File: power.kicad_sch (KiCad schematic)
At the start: 14 parts

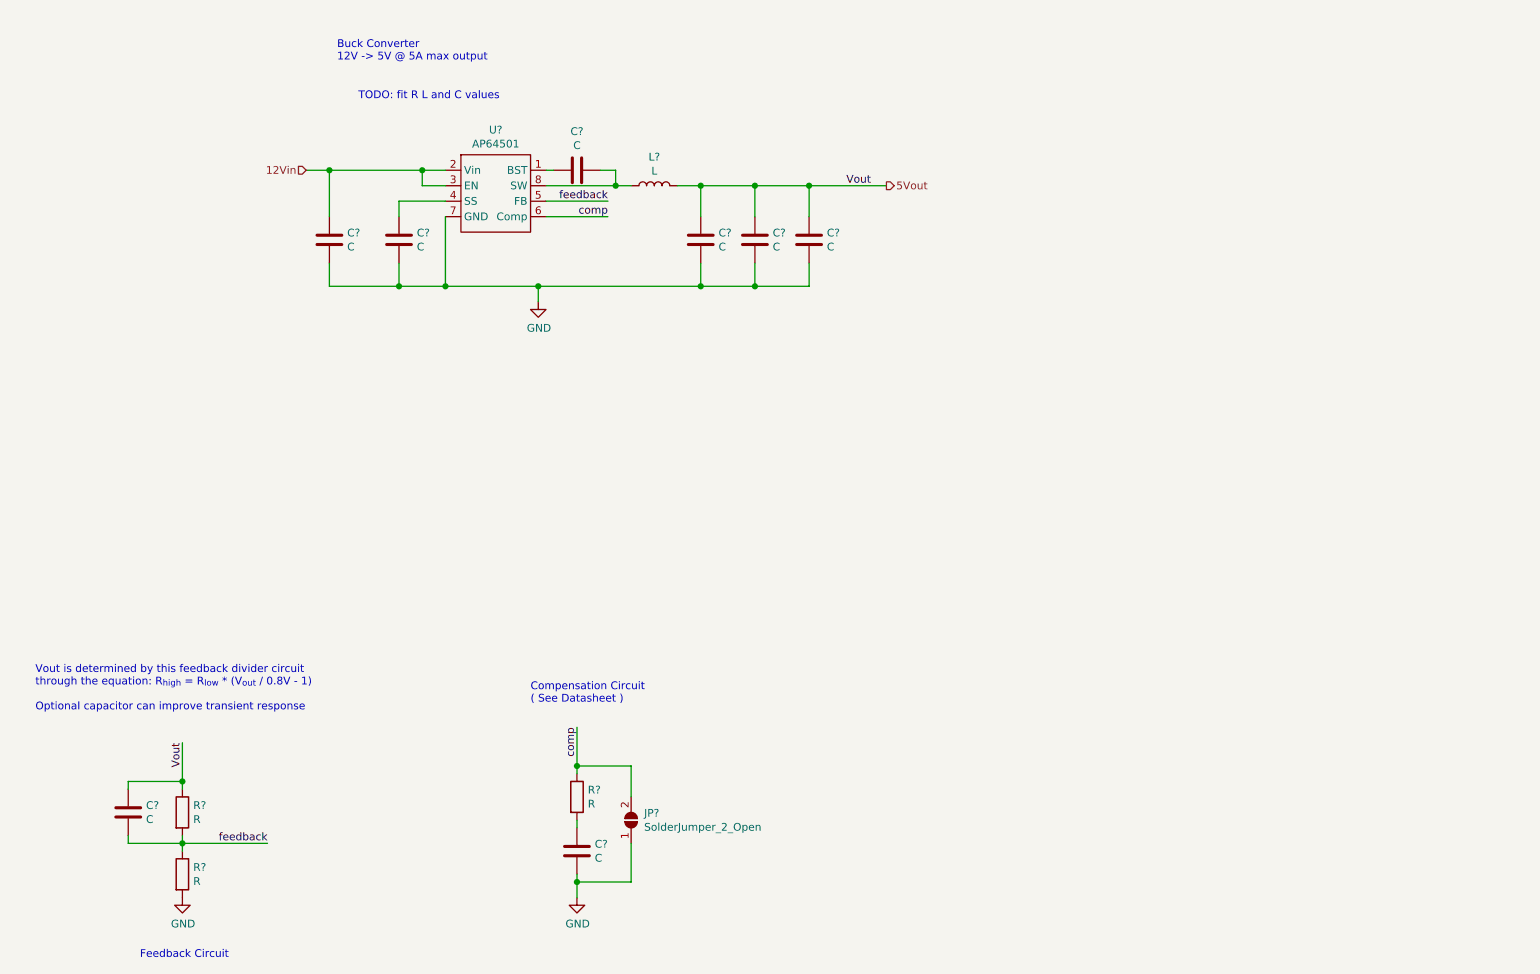
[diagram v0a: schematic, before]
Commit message: Added LC values and inductor part number to buck converter circuit
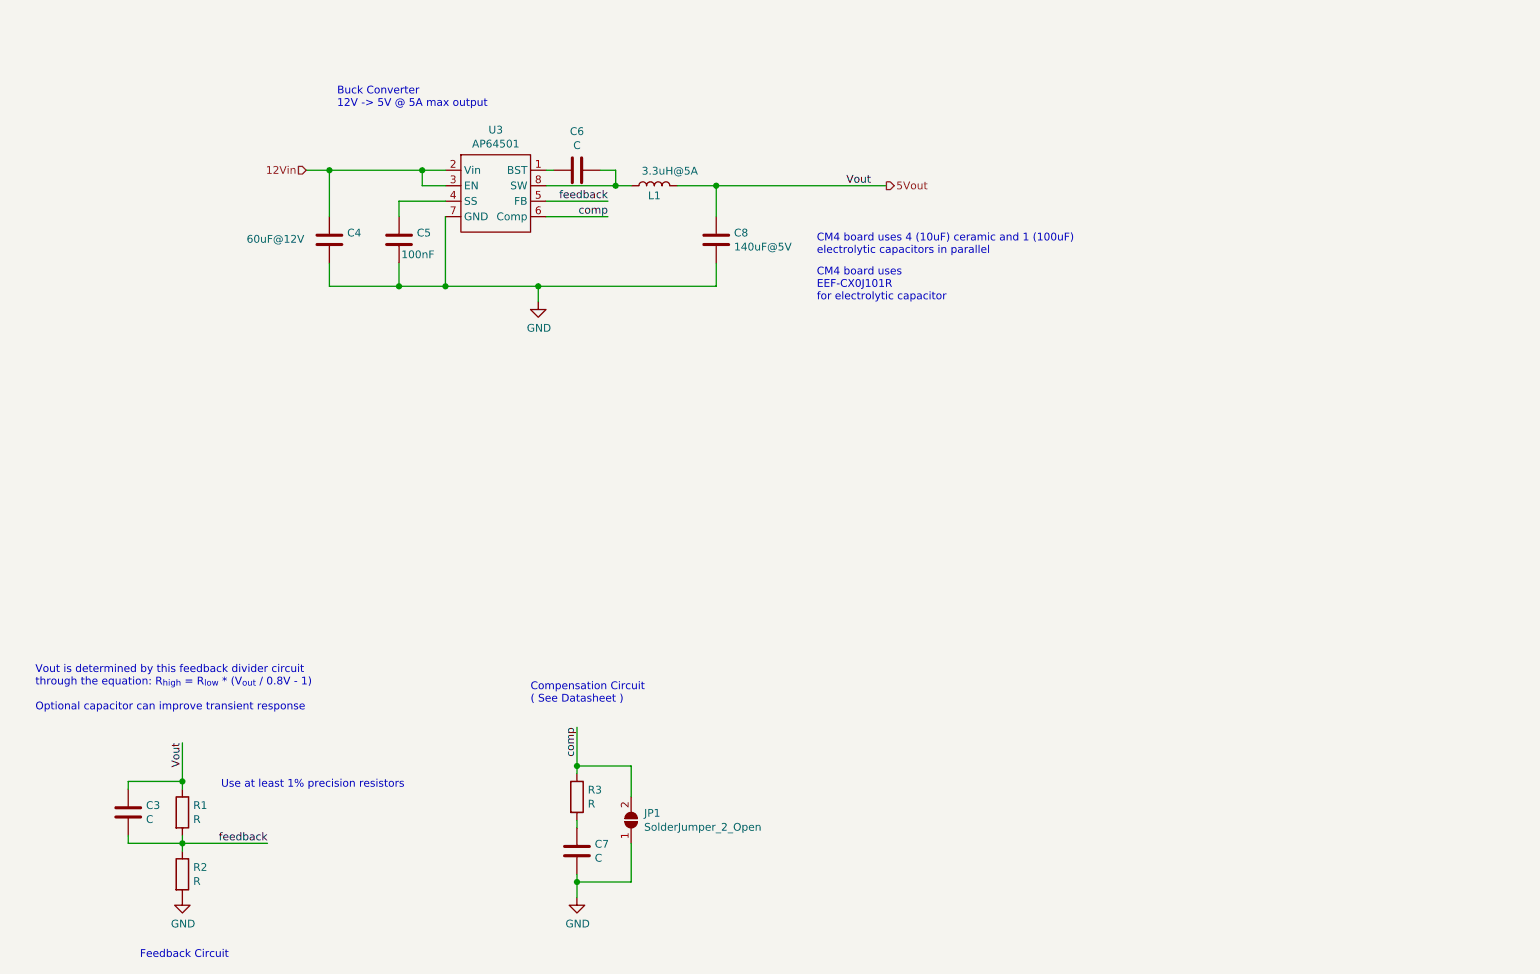
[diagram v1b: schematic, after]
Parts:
- removed C? (x2): C, symbol Device:C
- removed L?: L, symbol Device:L
- added L1: 3.3uH@5A, symbol symbols:3.3uH
- C4: renamed from C?; value C -> 60uF@12V
- C5: renamed from C?; value C -> 100nF
- C8: renamed from C?; value C -> 140uF@5V
- gave numbers to parts that had none: 8
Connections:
- net 5Vout: now also L1.2
- net at C6.2, U3.8 (SW): now also L1.1
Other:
- note added: "CM4 board uses 4 (10uF) ceramic and 1 (100uF) electrolytic capacitors in parallel"
- note added: "CM4 board uses EEF-CX0J101R for electrolytic capacitor"
- note added: "Use at least 1% precision resistors"
- note removed: "TODO: fit R L and C values"
- moved on the sheet: C8

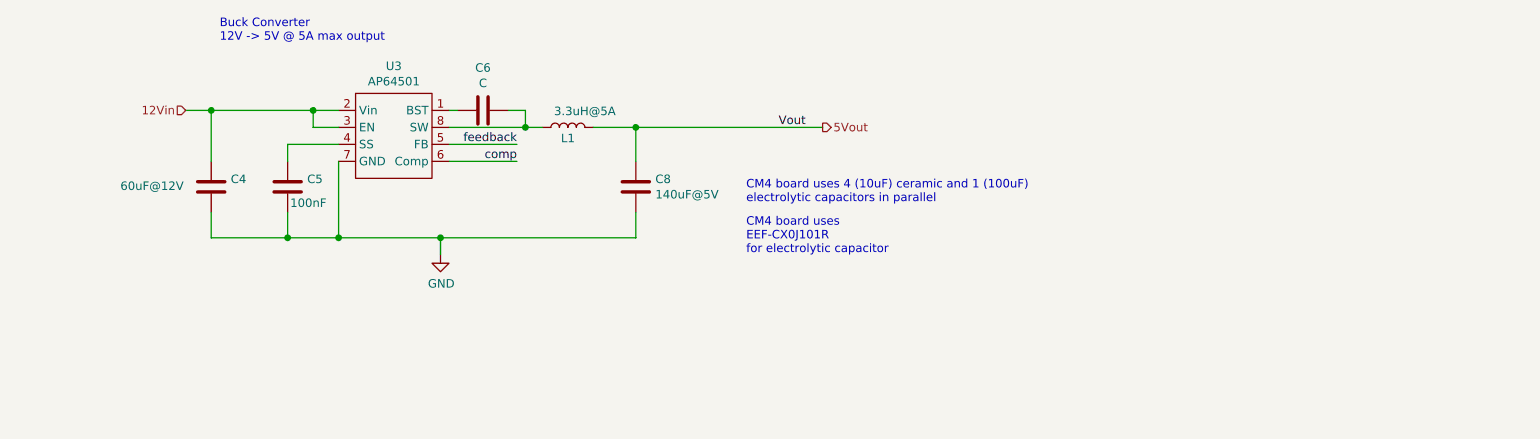
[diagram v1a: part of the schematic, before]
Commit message: visual tweaks to schematic
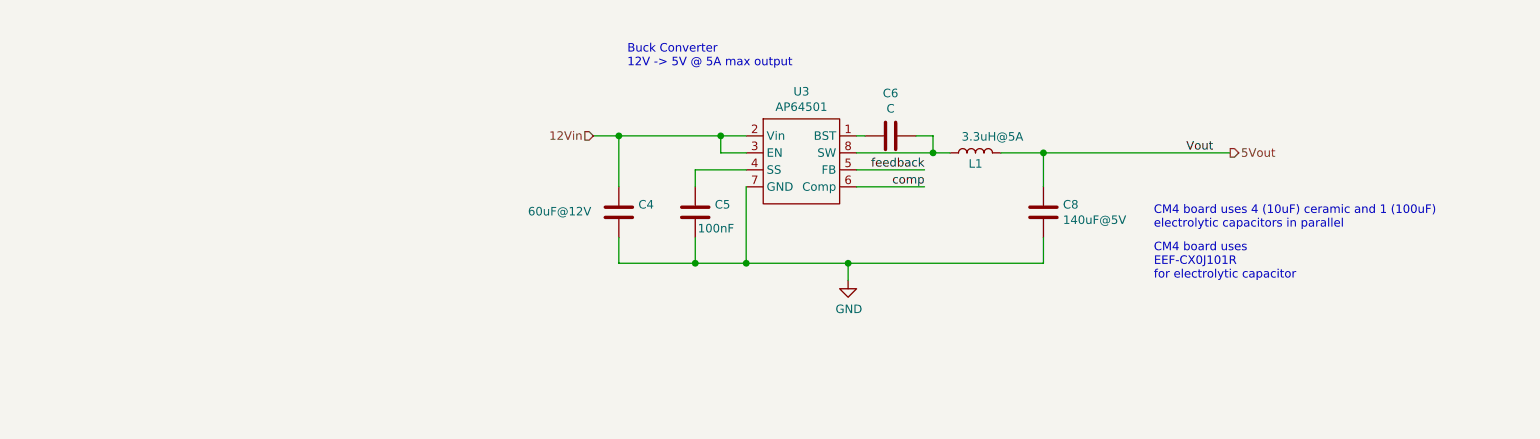
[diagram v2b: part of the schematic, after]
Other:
- moved on the sheet: C4, C5, C6, C8, L1, U3

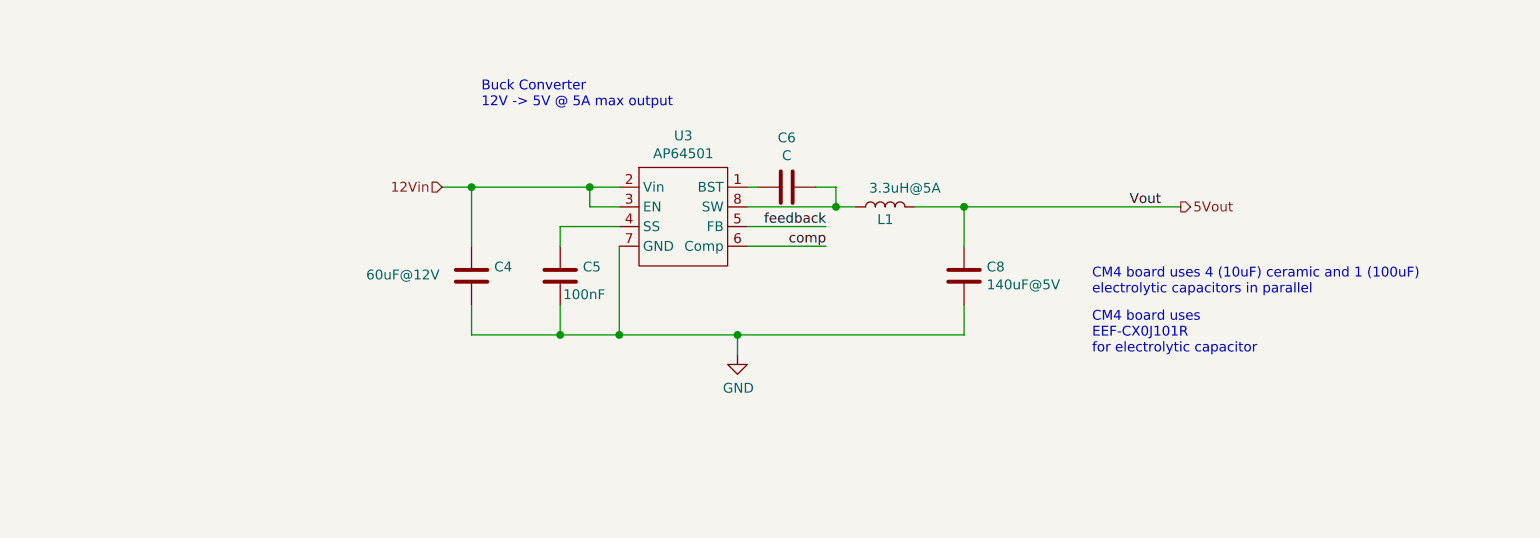
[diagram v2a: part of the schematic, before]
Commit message: Added buses and USB ports to schematic
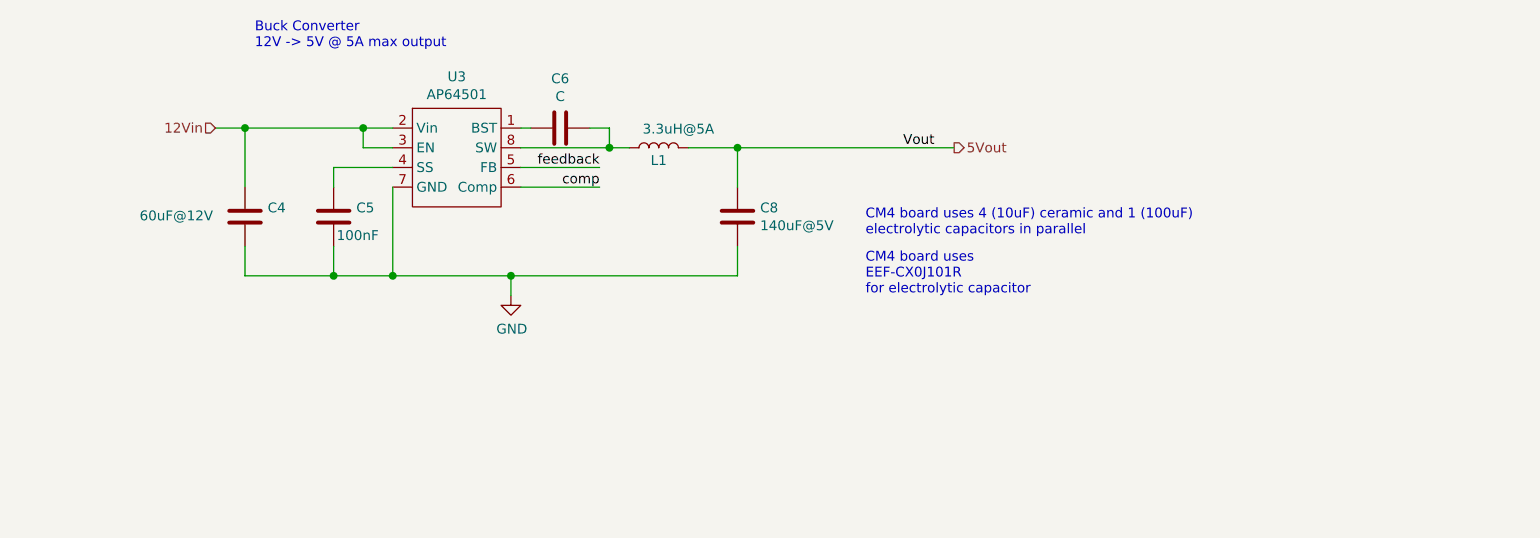
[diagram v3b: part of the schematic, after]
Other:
- company: (none) -> eCafe Racer
- title: (none) -> Dennis
- moved on the sheet: C4, C5, C6, C8, L1, U3

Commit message: footprints
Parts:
- added J5: Barrel_Jack, symbol Connector:Barrel_Jack
- C4: renamed from C3; footprint (none) -> Capacitor_SMD:C_0805_2012Metric
- C6: renamed from C7; footprint (none) -> Capacitor_SMD:C_0805_2012Metric
- C8: renamed from C6; footprint (none) -> Capacitor_SMD:C_0805_2012Metric
- R6: renamed from R1; footprint (none) -> Resistor_SMD:R_0805_2012Metric
- R7: renamed from R2; footprint (none) -> Resistor_SMD:R_0805_2012Metric
- R8: renamed from R3; footprint (none) -> Resistor_SMD:R_0805_2012Metric
- renumbered JP1 to JP4
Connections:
- net GND: now also J5.2
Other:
- note added: "External Power"
- note added: "TODO: - Bus power input (From DC to DC converter in battery - Bus power delivery"
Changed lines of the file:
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@@
+    (stroke (width 0) (type solid) (color 0 0 0 0))
+  )
+  (wire (pts (xy 41.91 34.29) (xy 44.45 34.29))
+    (stroke (width 0) (type solid) (color 0 0 0 0))
+  )
+  (wire (pts (xy 41.91 39.37) (xy 44.45 39.37))
+    (stroke (width 0) (type solid) (color 0 0 0 0))
+  )
+  (wire (pts (xy 44.45 31.75) (xy 44.45 34.29))
+    (stroke (width 0) (type solid) (color 0 0 0 0))
+  )
+  (wire (pts (xy 44.45 39.37) (xy 44.45 41.91))
     (stroke (width 0) (type solid) (color 0 0 0 0))
   )
@@
   (wire (pts (xy 168.91 68.58) (xy 168.91 64.77))
     (stroke (width 0) (type solid) (color 0 0 0 0))
+  )
+  (text "TODO:\n - Bus power input (From DC to DC converter in battery\n - Bus power delivery"
+    (at 22.86 60.96 0)
+    (effects (font (size 1.27 1.27)) (justify left bottom))
   )
   (text "Vout is determined by this feedback divider circuit\nthrough the equation: R_{high} = R_{low} * (V_{out} / 0.8V - 1)\n\nOptional capacitor can improve transient response"
     (at 25.4 142.24 0)
     (effects (font (size 1.27 1.27)) (justify left bottom))
+  )
+  (text "External Power" (at 39.37 45.72 180)
+    (effects (font (size 1.27 1.27)) (justify right bottom))
   )
   (text "Use at least 1% precision resistors" (at 55.88 154.94 0)
@@
     )
   )
+  (symbol (lib_id "power:GND") (at 44.45 41.91 0) (unit 1)
+    (in_bom yes) (on_board yes)
+    (property "Reference" "#PWR0118" (id 0) (at 44.45 48.26 0)
+      (effects (font (size 1.27 1.27)) hide)
+    )
+    (property "Value" "GND" (id 1) (at 44.5643 46.2344 0))
+    (property "Footprint" "" (id 2) (at 44.45 41.91 0)
+      (effects (font (size 1.27 1.27)) hide)
+    )
+    (property "Datasheet" "" (id 3) (at 44.45 41.91 0)
+      (effects (font (size 1.27 1.27)) hide)
+    )
+  )
   (symbol (lib_id "power:GND") (at 49.53 172.72 0) (unit 1)
     (in_bom yes) (on_board yes)
-    (property "Reference" "#PWR01" (id 0) (at 49.53 179.07 0)
+    (property "Reference" "#PWR0116" (id 0) (at 49.53 179.07 0)
       (effects (font (size 1.27 1.27)) hide)
     )
@@
   (symbol (lib_id "power:GND") (at 114.3 172.72 0) (unit 1)
     (in_bom yes) (on_board yes)
-    (property "Reference" "#PWR03" (id 0) (at 114.3 179.07 0)
+    (property "Reference" "#PWR0115" (id 0) (at 114.3 179.07 0)
       (effects (font (size 1.27 1.27)) hide)
     )
@@
   (symbol (lib_id "power:GND") (at 139.7 71.12 0) (unit 1)
     (in_bom yes) (on_board yes)
-    (property "Reference" "#PWR02" (id 0) (at 139.7 77.47 0)
+    (property "Reference" "#PWR0119" (id 0) (at 139.7 77.47 0)
       (effects (font (size 1.27 1.27)) hide)
     )
@@
   (symbol (lib_id "Device:R") (at 49.53 158.75 0) (unit 1)
     (in_bom yes) (on_board yes)
-    (property "Reference" "R1" (id 0) (at 51.3081 157.6006 0)
+    (property "Reference" "R6" (id 0) (at 51.3081 157.6006 0)
       (effects (font (size 1.27 1.27)) (justify left))
     )
@@
       (effects (font (size 1.27 1.27)) (justify left))
     )
-    (property "Footprint" "" (id 2) (at 47.752 158.75 90)
+    (property "Footprint" "Resistor_SMD:R_0805_2012Metric" (id 2) (at 47.752 158.75 90)
       (effects (font (size 1.27 1.27)) hide)
     )
@@
   (symbol (lib_id "Device:R") (at 49.53 168.91 0) (unit 1)
     (in_bom yes) (on_board yes)
-    (property "Reference" "R2" (id 0) (at 51.3081 167.7606 0)
+    (property "Reference" "R7" (id 0) (at 51.3081 167.7606 0)
       (effects (font (size 1.27 1.27)) (justify left))
     )
@@
       (effects (font (size 1.27 1.27)) (justify left))
     )
-    (property "Footprint" "" (id 2) (at 47.752 168.91 90)
+    (property "Footprint" "Resistor_SMD:R_0805_2012Metric" (id 2) (at 47.752 168.91 90)
       (effects (font (size 1.27 1.27)) hide)
     )
@@
   (symbol (lib_id "Device:R") (at 114.3 156.21 0) (unit 1)
     (in_bom yes) (on_board yes)
-    (property "Reference" "R3" (id 0) (at 116.0781 155.0606 0)
+    (property "Reference" "R8" (id 0) (at 116.0781 155.0606 0)
       (effects (font (size 1.27 1.27)) (justify left))
     )
@@
       (effects (font (size 1.27 1.27)) (justify left))
     )
-    (property "Footprint" "" (id 2) (at 112.522 156.21 90)
+    (property "Footprint" "Resistor_SMD:R_0805_2012Metric" (id 2) (at 112.522 156.21 90)
       (effects (font (size 1.27 1.27)) hide)
     )
@@
   (symbol (lib_id "Jumper:SolderJumper_2_Open") (at 123.19 160.02 90) (unit 1)
     (in_bom yes) (on_board yes)
-    (property "Reference" "JP1" (id 0) (at 125.3237 158.8706 90)
+    (property "Reference" "JP4" (id 0) (at 125.3237 158.8706 90)
       (effects (font (size 1.27 1.27)) (justify right))
     )
@@
   (symbol (lib_id "Device:C") (at 40.64 158.75 0) (unit 1)
     (in_bom yes) (on_board yes)
-    (property "Reference" "C3" (id 0) (at 43.5611 157.6006 0)
+    (property "Reference" "C4" (id 0) (at 43.5611 157.6006 0)
       (effects (font (size 1.27 1.27)) (justify left))
     )
@@
       (effects (font (size 1.27 1.27)) (justify left))
     )
-    (property "Footprint" "" (id 2) (at 41.6052 162.56 0)
+    (property "Footprint" "Capacitor_SMD:C_0805_2012Metric" (id 2) (at 41.6052 162.56 0)
       (effects (font (size 1.27 1.27)) hide)
     )
@@
   (symbol (lib_id "Device:C") (at 114.3 165.1 0) (unit 1)
     (in_bom yes) (on_board yes)
-    (property "Reference" "C7" (id 0) (at 117.2211 163.9506 0)
+    (property "Reference" "C6" (id 0) (at 117.2211 163.9506 0)
       (effects (font (size 1.27 1.27)) (justify left))
     )
@@
       (effects (font (size 1.27 1.27)) (justify left))
     )
-    (property "Footprint" "" (id 2) (at 115.2652 168.91 0)
+    (property "Footprint" "Capacitor_SMD:C_0805_2012Metric" (id 2) (at 115.2652 168.91 0)
       (effects (font (size 1.27 1.27)) hide)
     )
@@
   (symbol (lib_id "Device:C") (at 146.05 49.53 90) (unit 1)
     (in_bom yes) (on_board yes)
-    (property "Reference" "C6" (id 0) (at 146.05 43.1608 90))
+    (property "Reference" "C8" (id 0) (at 146.05 43.1608 90))
     (property "Value" "C" (id 1) (at 146.05 45.4595 90))
-    (property "Footprint" "" (id 2) (at 149.86 48.5648 0)
+    (property "Footprint" "Capacitor_SMD:C_0805_2012Metric" (id 2) (at 149.86 48.5648 0)
       (effects (font (size 1.27 1.27)) hide)
     )
@@
       (effects (font (size 1.27 1.27)) hide)
     )
+  )
+  (symbol (lib_id "Connector:Barrel_Jack") (at 34.29 36.83 0) (unit 1)
+    (in_bom yes) (on_board yes)
+    (property "Reference" "J5" (id 0) (at 35.687 28.7082 0))
+    (property "Value" "Barrel_Jack" (id 1) (at 35.687 31.0069 0))
+    (property "Footprint" "" (id 2) (at 35.56 37.846 0)
+      (effects (font (size 1.27 1.27)) hide)
+    )
+    (property "Datasheet" "~" (id 3) (at 35.56 37.846 0)
+      (effects (font (size 1.27 1.27)) hide)
+    )
